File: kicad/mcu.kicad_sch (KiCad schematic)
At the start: 1 part, among them U1 ESP32-C6-DEVKITC-1-N8

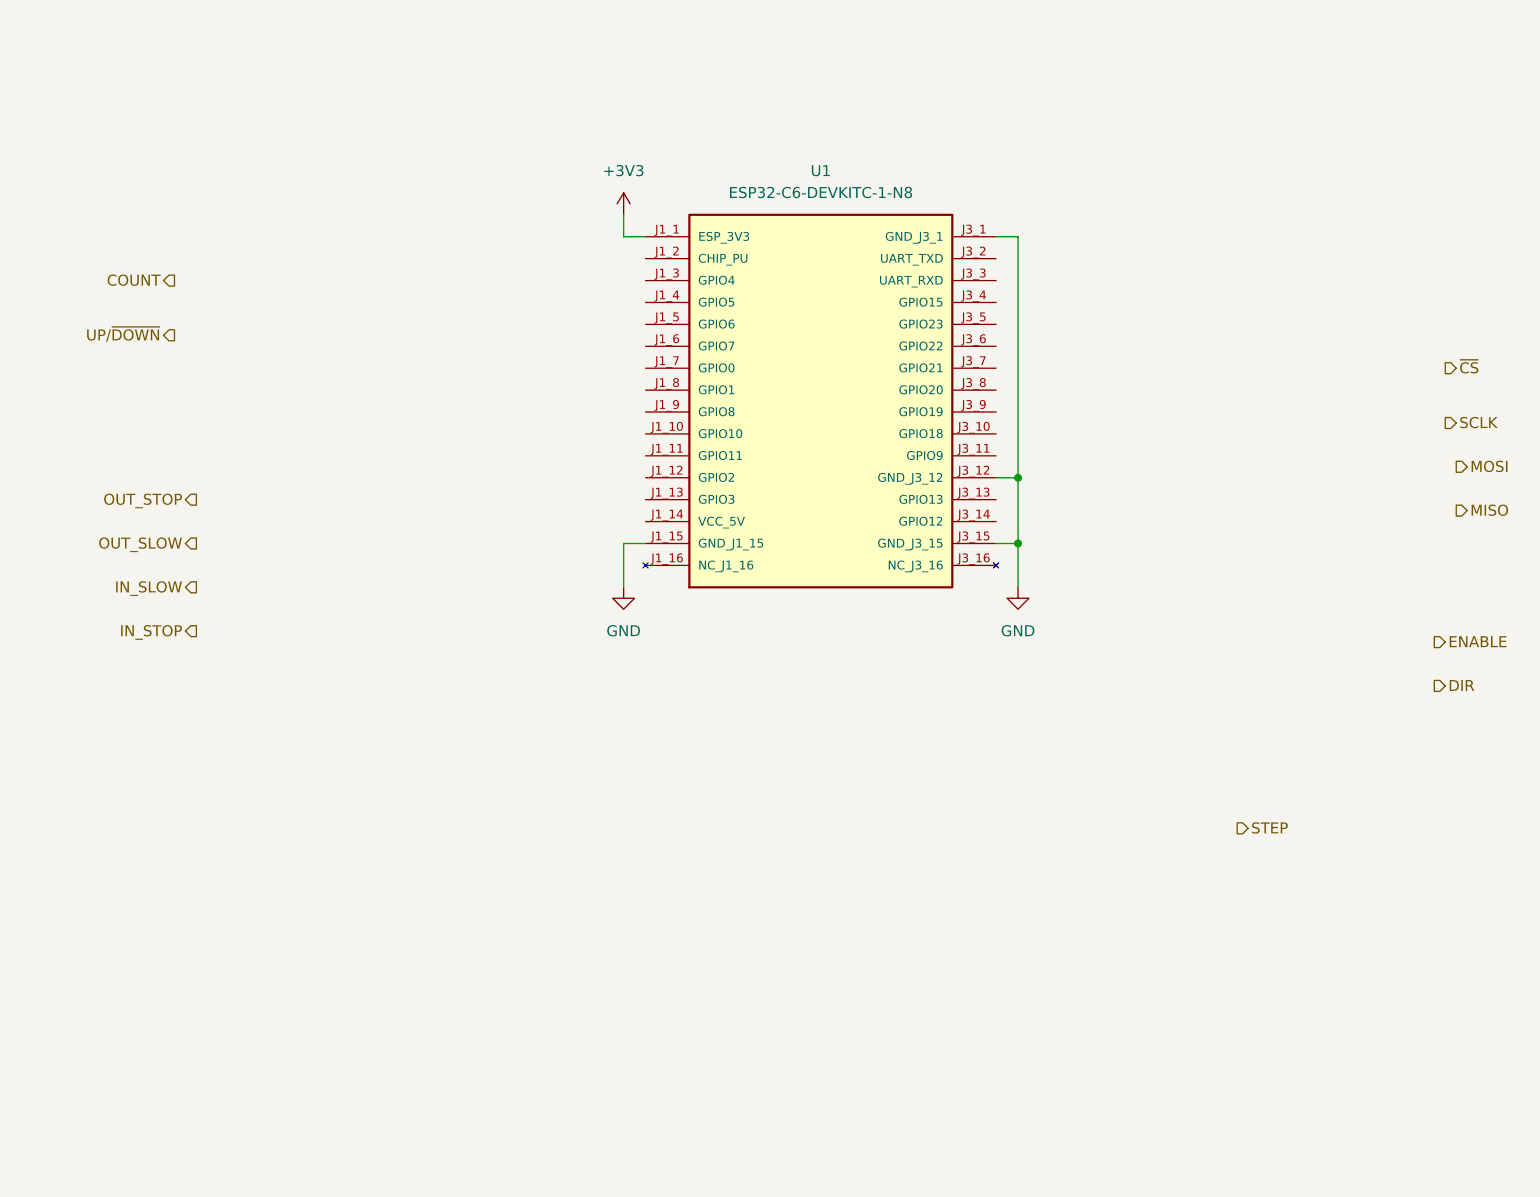
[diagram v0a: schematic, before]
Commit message: Completed the schematic. All components have Digikey part numbers and footprints. The power supply sheet still requires some work.
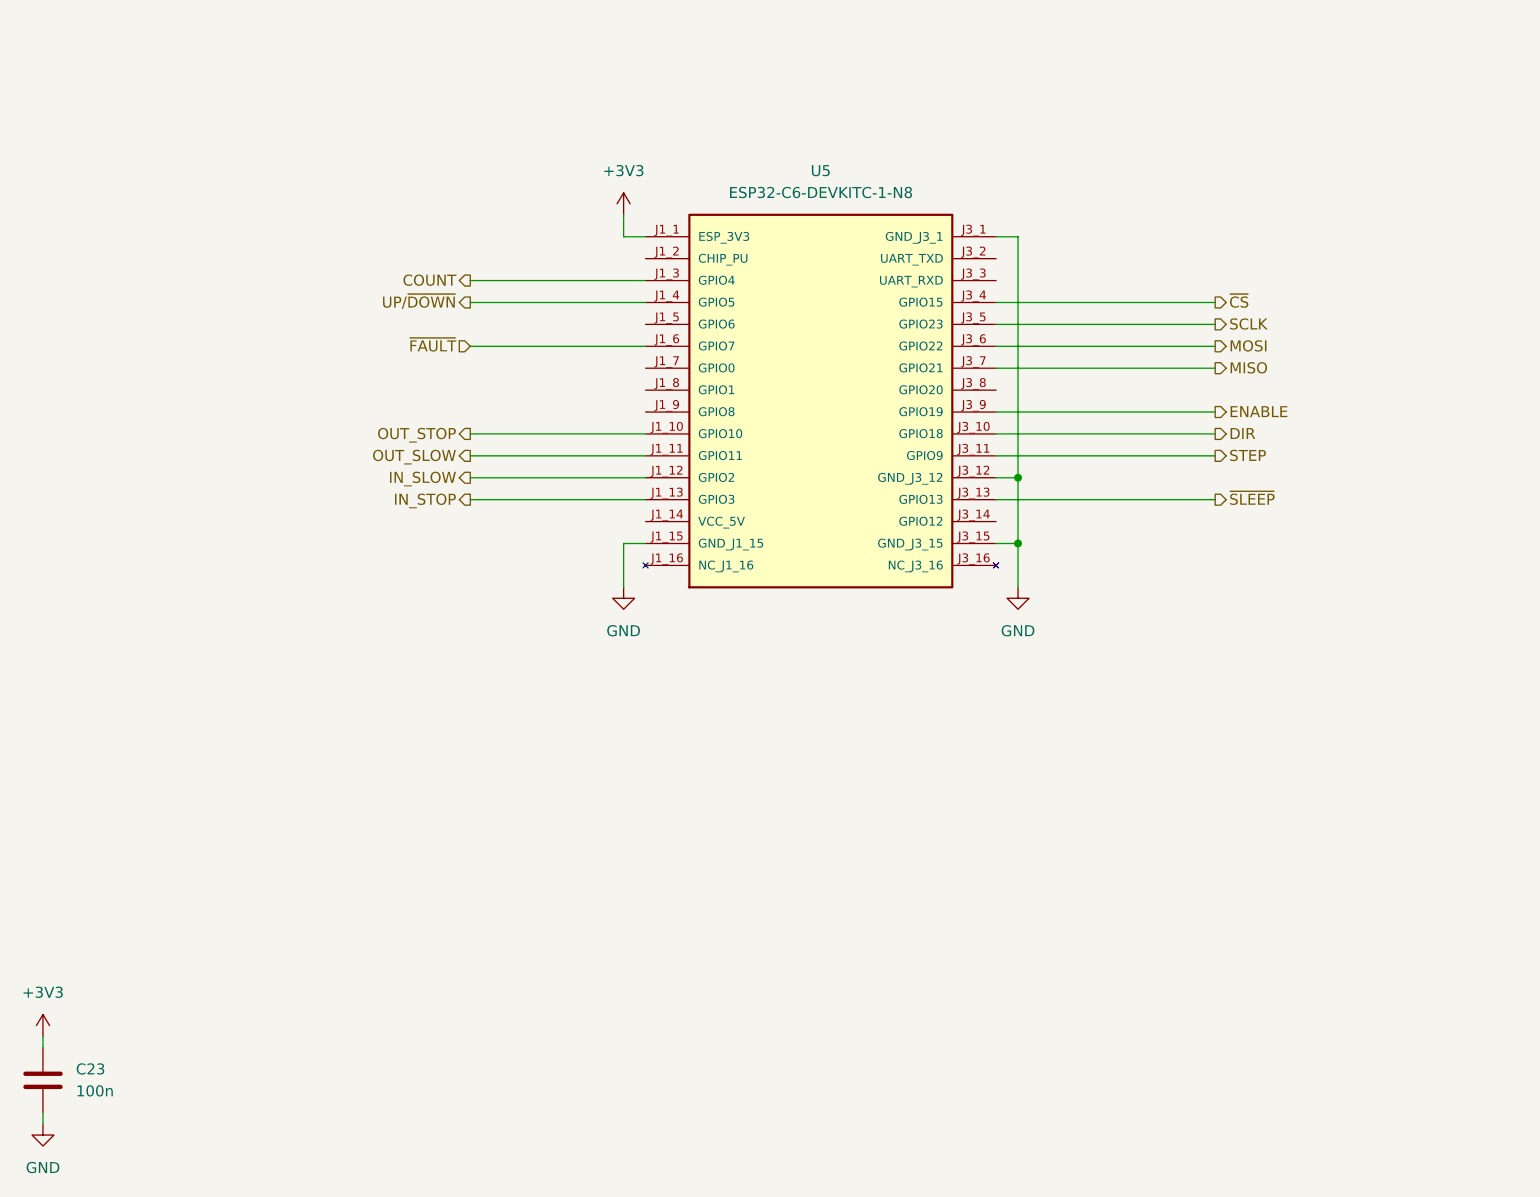
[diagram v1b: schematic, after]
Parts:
- added C23: 100n, Capacitor_SMD:C_0603_1608Metric, symbol Device:C
- U5: renamed from U1; MF (none) -> Espressif; MP (none) -> ESP32-C6-DEVKITC-1-N8; Supplier (none) -> Digi-Key; SupplierPN (none) -> 1965-ESP32-C6-DEVKITC-1-N8-ND
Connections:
- net +3V3: now also C23.1
- net COUNT: now also U5.J1_3 (GPIO4)
- net DIR: now also U5.J3_10 (GPIO18)
- net ENABLE: now also U5.J3_9 (GPIO19)
- net GND: now also C23.2
- net IN_SLOW: now also U5.J1_12 (GPIO2)
- net IN_STOP: now also U5.J1_13 (GPIO3)
- net MISO: now also U5.J3_7 (GPIO21)
- net MOSI: now also U5.J3_6 (GPIO22)
- net OUT_SLOW: now also U5.J1_11 (GPIO11)
- net OUT_STOP: now also U5.J1_10 (GPIO10)
- net SCLK: now also U5.J3_5 (GPIO23)
- net STEP: now also U5.J3_11 (GPIO9)
- net UP/~{DOWN}: now also U5.J1_4 (GPIO5)
- net ~{CS}: now also U5.J3_4 (GPIO15)
- net ~{FAULT}: now reaches U5.J1_6 (GPIO7)
- net ~{SLEEP}: now reaches U5.J3_13 (GPIO13)
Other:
- company: (none) -> NX Solutions
- title: (none) -> TV slider

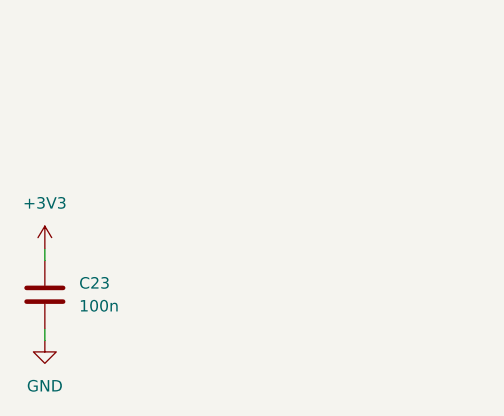
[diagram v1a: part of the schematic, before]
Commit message: Updated footprints and step models. Placed on PCB, but not yet positioned in final location.
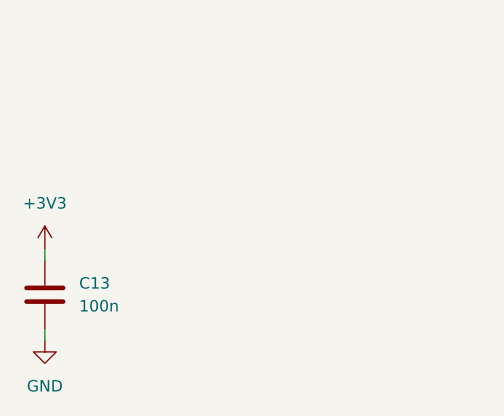
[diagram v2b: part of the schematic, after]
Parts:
- C13: renamed from C23; SupplierPN 490-3890-1-ND -> 490-3285-1-ND
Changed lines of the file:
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@@
 		(dnp no)
 		(fields_autoplaced yes)
-		(property "Reference" "#PWR040"
+		(property "Reference" "#PWR043"
 			(at 166.37 123.19 0)
 			(effects
@@
 			(project ""
 				(path "/914c4b67-a7a4-47f3-8515-668040fd3f8c/29d09a3f-5d85-4167-9532-6c777b8bdc81"
-					(reference "#PWR040")
+					(reference "#PWR043")
 					(unit 1)
 				)
@@
 		(dnp no)
 		(fields_autoplaced yes)
-		(property "Reference" "#PWR075"
+		(property "Reference" "#PWR039"
 			(at 53.34 172.72 0)
 			(effects
@@
 			(project "tv_slider"
 				(path "/914c4b67-a7a4-47f3-8515-668040fd3f8c/29d09a3f-5d85-4167-9532-6c777b8bdc81"
-					(reference "#PWR075")
+					(reference "#PWR039")
 					(unit 1)
 				)
@@
 		(dnp no)
 		(fields_autoplaced yes)
-		(property "Reference" "#PWR038"
+		(property "Reference" "#PWR041"
 			(at 120.65 77.47 0)
 			(effects
@@
 			(project ""
 				(path "/914c4b67-a7a4-47f3-8515-668040fd3f8c/29d09a3f-5d85-4167-9532-6c777b8bdc81"
-					(reference "#PWR038")
+					(reference "#PWR041")
 					(unit 1)
 				)
@@
 		(dnp no)
 		(fields_autoplaced yes)
-		(property "Reference" "#PWR039"
+		(property "Reference" "#PWR042"
 			(at 120.65 123.19 0)
 			(effects
@@
 			(project ""
 				(path "/914c4b67-a7a4-47f3-8515-668040fd3f8c/29d09a3f-5d85-4167-9532-6c777b8bdc81"
-					(reference "#PWR039")
+					(reference "#PWR042")
 					(unit 1)
 				)
@@
 		(dnp no)
 		(fields_autoplaced yes)
-		(property "Reference" "C23"
+		(property "Reference" "C13"
 			(at 57.15 172.7199 0)
 			(effects
@@
 			)
 		)
-		(property "SupplierPN" "490-3890-1-ND"
+		(property "SupplierPN" "490-3285-1-ND"
 			(at 53.34 173.99 0)
 			(effects
@@
 			(project "tv_slider"
 				(path "/914c4b67-a7a4-47f3-8515-668040fd3f8c/29d09a3f-5d85-4167-9532-6c777b8bdc81"
-					(reference "C23")
+					(reference "C13")
 					(unit 1)
 				)
@@
 		(dnp no)
 		(fields_autoplaced yes)
-		(property "Reference" "#PWR074"
+		(property "Reference" "#PWR040"
 			(at 53.34 185.42 0)
 			(effects
@@
 			(project "tv_slider"
 				(path "/914c4b67-a7a4-47f3-8515-668040fd3f8c/29d09a3f-5d85-4167-9532-6c777b8bdc81"
-					(reference "#PWR074")
-					(unit 1)
-				)
+					(reference "#PWR040")
+					(unit 1)
+				)

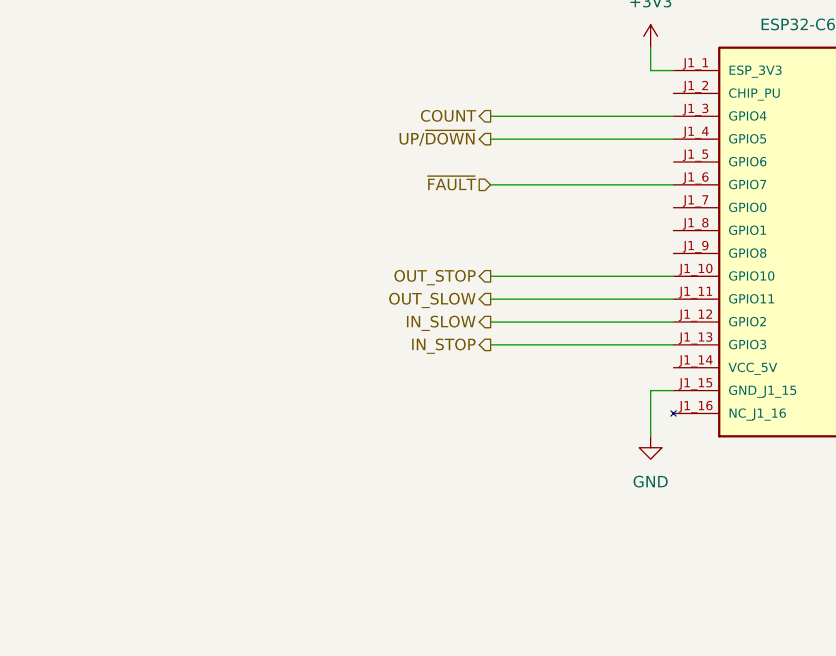
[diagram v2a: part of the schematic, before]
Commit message: Updated all schematic pages except the power supply. Did the initial component placement.
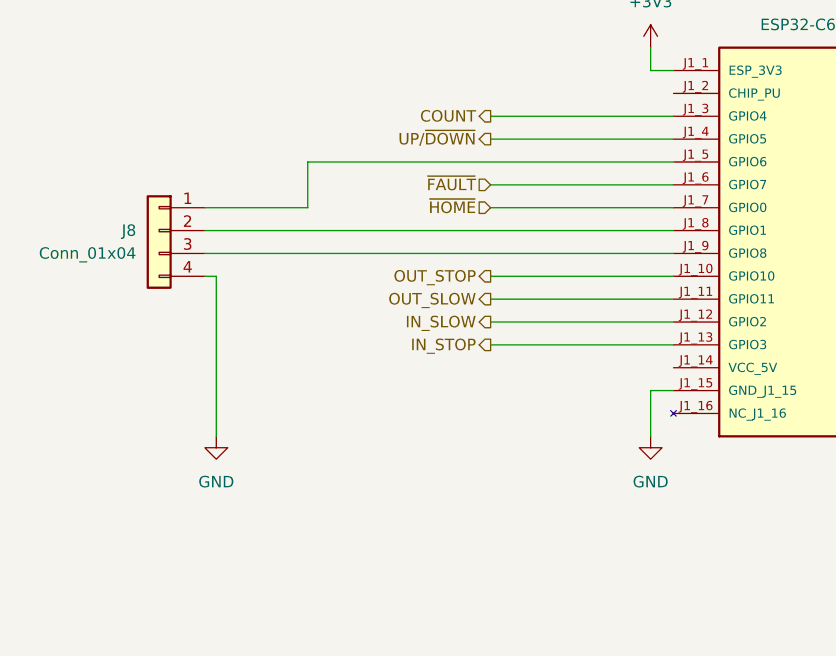
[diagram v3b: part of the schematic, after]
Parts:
- added J8: Conn_01x04, Connector_PinHeader_2.54mm:PinHeader_1x04_P2.54mm_Vertical, symbol Connector_Generic:Conn_01x04
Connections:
- net GND: now also J8.4 (Pin_4)
- net at U5.J1_5 (GPIO6): now also J8.1 (Pin_1)
- net ~{HOME}: now reaches U5.J1_7 (GPIO0)
- net at U5.J1_8 (GPIO1): now also J8.2 (Pin_2)
- net at U5.J1_9 (GPIO8): now also J8.3 (Pin_3)
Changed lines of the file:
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@@
+	(wire
+		(pts
+			(xy 82.55 91.44) (xy 71.12 91.44)
+		)
+		(stroke
+			(width 0)
+			(type default)
+		)
+	)
+	(wire
+		(pts
+			(xy 102.87 91.44) (xy 123.19 91.44)
+		)
+		(stroke
+			(width 0)
+			(type default)
+		)
+	)
 	(wire
 		(pts
@@
 	(wire
 		(pts
+			(xy 82.55 86.36) (xy 82.55 91.44)
+		)
+		(stroke
+			(width 0)
+			(type default)
+		)
+	)
+	(wire
+		(pts
 			(xy 102.87 104.14) (xy 123.19 104.14)
 		)
@@
 	(wire
 		(pts
+			(xy 71.12 96.52) (xy 123.19 96.52)
+		)
+		(stroke
+			(width 0)
+			(type default)
+		)
+	)
+	(wire
+		(pts
 			(xy 163.83 83.82) (xy 189.23 83.82)
 		)
@@
 	(wire
 		(pts
+			(xy 123.19 86.36) (xy 82.55 86.36)
+		)
+		(stroke
+			(width 0)
+			(type default)
+		)
+	)
+	(wire
+		(pts
 			(xy 163.83 101.6) (xy 189.23 101.6)
 		)
@@
 	(wire
 		(pts
+			(xy 72.39 99.06) (xy 71.12 99.06)
+		)
+		(stroke
+			(width 0)
+			(type default)
+		)
+	)
+	(wire
+		(pts
+			(xy 72.39 116.84) (xy 72.39 99.06)
+		)
+		(stroke
+			(width 0)
+			(type default)
+		)
+	)
+	(wire
+		(pts
 			(xy 102.87 106.68) (xy 123.19 106.68)
 		)
@@
 	(wire
 		(pts
+			(xy 71.12 93.98) (xy 123.19 93.98)
+		)
+		(stroke
+			(width 0)
+			(type default)
+		)
+	)
+	(wire
+		(pts
 			(xy 163.83 86.36) (xy 189.23 86.36)
 		)
@@
 			(width 0)
 			(type default)
+		)
+	)
+	(hierarchical_label "~{HOME}"
+		(shape input)
+		(at 102.87 91.44 180)
+		(effects
+			(font
+				(size 1.27 1.27)
+			)
+			(justify right)
 		)
 	)
@@
 		(dnp no)
 		(fields_autoplaced yes)
-		(property "Reference" "#PWR043"
+		(property "Reference" "#PWR036"
 			(at 166.37 123.19 0)
 			(effects
@@
 			(project ""
 				(path "/914c4b67-a7a4-47f3-8515-668040fd3f8c/29d09a3f-5d85-4167-9532-6c777b8bdc81"
-					(reference "#PWR043")
+					(reference "#PWR036")
+					(unit 1)
+				)
+			)
+		)
+	)
+	(symbol
+		(lib_id "power:GND")
+		(at 72.39 116.84 0)
+		(unit 1)
+		(exclude_from_sim no)
+		(in_bom yes)
+		(on_board yes)
+		(dnp no)
+		(fields_autoplaced yes)
+		(property "Reference" "#PWR038"
+			(at 72.39 123.19 0)
+			(effects
+				(font
+					(size 1.27 1.27)
+				)
+				(hide yes)
+			)
+		)
+		(property "Value" "GND"
+			(at 72.39 121.92 0)
+			(effects
+				(font
+					(size 1.27 1.27)
+				)
+			)
+		)
+		(property "Footprint" ""
+			(at 72.39 116.84 0)
+			(effects
+				(font
+					(size 1.27 1.27)
+				)
+				(hide yes)
+			)
+		)
+		(property "Datasheet" ""
+			(at 72.39 116.84 0)
+			(effects
+				(font
+					(size 1.27 1.27)
+				)
+				(hide yes)
+			)
+		)
+		(property "Description" "Power symbol creates a global label with name \"GND\" , ground"
+			(at 72.39 116.84 0)
+			(effects
+				(font
+					(size 1.27 1.27)
+				)
+				(hide yes)
+			)
+		)
+		(pin "1"
+		)
+		(instances
+			(project "tv_slider"
+				(path "/914c4b67-a7a4-47f3-8515-668040fd3f8c/29d09a3f-5d85-4167-9532-6c777b8bdc81"
+					(reference "#PWR038")
 					(unit 1)
 				)
@@
 		(dnp no)
 		(fields_autoplaced yes)
-		(property "Reference" "#PWR039"
+		(property "Reference" "#PWR037"
 			(at 53.34 172.72 0)
 			(effects
@@
 			(project "tv_slider"
 				(path "/914c4b67-a7a4-47f3-8515-668040fd3f8c/29d09a3f-5d85-4167-9532-6c777b8bdc81"
-					(reference "#PWR039")
+					(reference "#PWR037")
 					(unit 1)
 				)
@@
 		(dnp no)
 		(fields_autoplaced yes)
-		(property "Reference" "#PWR041"
+		(property "Reference" "#PWR034"
 			(at 120.65 77.47 0)
 			(effects
@@
 			(project ""
 				(path "/914c4b67-a7a4-47f3-8515-668040fd3f8c/29d09a3f-5d85-4167-9532-6c777b8bdc81"
-					(reference "#PWR041")
+					(reference "#PWR034")
 					(unit 1)
 				)
@@
 		(dnp no)
 		(fields_autoplaced yes)
-		(property "Reference" "#PWR042"
+		(property "Reference" "#PWR035"
 			(at 120.65 123.19 0)
 			(effects
@@
 			(project ""
 				(path "/914c4b67-a7a4-47f3-8515-668040fd3f8c/29d09a3f-5d85-4167-9532-6c777b8bdc81"
-					(reference "#PWR042")
+					(reference "#PWR035")
+					(unit 1)
+				)
+			)
+		)
+	)
+	(symbol
+		(lib_id "Connector_Generic:Conn_01x04")
+		(at 66.04 93.98 0)
+		(mirror y)
+		(unit 1)
+		(exclude_from_sim no)
+		(in_bom yes)
+		(on_board yes)
+		(dnp no)
+		(property "Reference" "J8"
+			(at 63.5 93.9799 0)
+			(effects
+				(font
+					(size 1.27 1.27)
+				)
+				(justify left)
+			)
+		)
+		(property "Value" "Conn_01x04"
+			(at 63.5 96.5199 0)
+			(effects
+				(font
+					(size 1.27 1.27)
+				)
+				(justify left)
+			)
+		)
+		(property "Footprint" "Connector_PinHeader_2.54mm:PinHeader_1x04_P2.54mm_Vertical"
+			(at 66.04 93.98 0)
+			(effects
+				(font
+					(size 1.27 1.27)
+				)
+				(hide yes)
+			)
+		)
+		(property "Datasheet" "~"
+			(at 66.04 93.98 0)
+			(effects
+				(font
+					(size 1.27 1.27)
+				)
+				(hide yes)
+			)
+		)
+		(property "Description" "Generic connector, single row, 01x04, script generated (kicad-library-utils/schlib/autogen/connector/)"
+			(at 66.04 93.98 0)
+			(effects
+				(font
+					(size 1.27 1.27)
+				)
+				(hide yes)
+			)
+		)
+		(pin "1"
+		)
+		(pin "4"
+		)
+		(pin "3"
+		)
+		(pin "2"
+		)
+		(instances
+			(project ""
+				(path "/914c4b67-a7a4-47f3-8515-668040fd3f8c/29d09a3f-5d85-4167-9532-6c777b8bdc81"
+					(reference "J8")
 					(unit 1)
 				)
@@
 		(dnp no)
 		(fields_autoplaced yes)
-		(property "Reference" "#PWR040"
+		(property "Reference" "#PWR039"
 			(at 53.34 185.42 0)
 			(effects
@@
 			(project "tv_slider"
 				(path "/914c4b67-a7a4-47f3-8515-668040fd3f8c/29d09a3f-5d85-4167-9532-6c777b8bdc81"
-					(reference "#PWR040")
+					(reference "#PWR039")
 					(unit 1)
 				)
